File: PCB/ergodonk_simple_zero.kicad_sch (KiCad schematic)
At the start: 146 parts, among them J2 4PIN, Q1 TIP120, SW0 SW_PUSH_LED, SW08_RH10 SW_PUSH_LED, SW1 SW_PUSH_LED, SW10 SW_PUSH_LED, SW11 SW_PUSH_LED, SW12 SW_PUSH_LED, SW13 SW_PUSH_LED, SW14 SW_PUSH_LED, SW15 SW_PUSH_LED, SW16 SW_PUSH_LED, SW17 SW_PUSH_LED, SW18_RH10 SW_PUSH_LED, SW2 SW_PUSH_LED, SW20 SW_PUSH_LED, SW21 SW_PUSH_LED, SW22 SW_PUSH_LED, SW23 SW_PUSH_LED, SW24 SW_PUSH_LED, SW25 SW_PUSH_LED, SW26 SW_PUSH_LED, SW27 SW_PUSH_LED, SW28_RH10 SW_PUSH_LED, SW3 SW_PUSH_LED, SW30 SW_PUSH_LED, SW31 SW_PUSH_LED, SW32 SW_PUSH_LED, SW33 SW_PUSH_LED, SW34 SW_PUSH_LED, SW35 SW_PUSH_LED, SW36 SW_PUSH_LED, SW37 SW_PUSH_LED, SW38_RH10 SW_PUSH_LED, SW4 SW_PUSH_LED, SW40 SW_PUSH_LED, SW42 SW_PUSH_LED, SW43 SW_PUSH_LED, SW44 SW_PUSH_LED, SW45 SW_PUSH_LED, SW46 SW_PUSH_LED, SW47 SW_PUSH_LED, SW48_RH10 SW_PUSH_LED, SW5 SW_PUSH_LED, SW50 SW_PUSH_LED, SW51 SW_PUSH_LED, SW52 SW_PUSH_LED, SW53 SW_PUSH_LED, SW54 SW_PUSH_LED, SW55 SW_PUSH_LED, SW56 SW_PUSH_LED, SW57 SW_PUSH_LED, SW58 SW_PUSH_LED, SW6 SW_PUSH_LED, SW7 SW_PUSH_LED

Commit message: Added keycap labels updated RH exclusive component labels improved Solenoid circuit markings
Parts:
- J_SOL_1: footprint Connector_PinHeader_2.54mm:PinHeader_1x02_P2.54mm_Vertical -> Ergodonk_simple_zero:PinHeader_1x02_P2.54mm_Vertical
- R2: footprint Resistor_THT:R_Axial_DIN0309_L9.0mm_D3.2mm_P12.70mm_Horizontal -> Ergodonk_simple_zero:R_Axial_DIN0309_L9.0mm_D3.2mm_P12.70mm_Horizontal
- SW0: LH (none) -> VOL UP; RH (none) -> PRTSC
- SW08: renamed from SW08_RH10; RH (none) -> BKSP
- SW1: LH (none) -> F6; RH (none) -> F7
- SW10: LH (none) -> VOL DN; RH (none) -> SCRL
- SW11: LH (none) -> *; RH (none) -> INSERT
- SW12: LH (none) -> 5; RH (none) -> 6
- SW13: LH (none) -> 4; RH (none) -> 7
- SW14: LH (none) -> 3; RH (none) -> 8
- SW15: LH (none) -> 2; RH (none) -> 9
- SW16: LH (none) -> 1; RH (none) -> 0
- SW17: LH (none) -> `; RH (none) -> -
- SW18: renamed from SW18_RH10; RH (none) -> =
- SW2: LH (none) -> F5; RH (none) -> F8
- SW20: LH (none) -> MUTE; RH (none) -> PAUSE
- SW21: LH (none) -> PGUP; RH (none) -> DEL
- SW22: LH (none) -> T; RH (none) -> Y
- SW23: LH (none) -> R; RH (none) -> U
- SW24: LH (none) -> E; RH (none) -> I
- SW25: LH (none) -> W; RH (none) -> O
- SW26: LH (none) -> Q; RH (none) -> P
- SW27: LH (none) -> TAB; RH (none) -> [
- SW28: renamed from SW28_RH10; RH (none) -> \
- SW3: LH (none) -> F4; RH (none) -> F9
- SW30: LH (none) -> HOME; RH (none) -> PGUP
- SW31: LH (none) -> PGDN; RH (none) -> 5
- SW32: LH (none) -> G; RH (none) -> H
- SW33: LH (none) -> F; RH (none) -> I
- SW34: LH (none) -> D; RH (none) -> J
- SW35: LH (none) -> S; RH (none) -> K
- SW36: LH (none) -> A; RH (none) -> L
- SW37: LH (none) -> CAPS; RH (none) -> ;
- SW38: renamed from SW38_RH10; RH (none) -> ]
- SW4: LH (none) -> F3; RH (none) -> F10
- SW40: LH (none) -> END; RH (none) -> PGDN
- SW42: LH (none) -> B; RH (none) -> N
- SW43: LH (none) -> V; RH (none) -> M
- SW44: LH (none) -> C; RH (none) -> ,
- SW45: LH (none) -> X; RH (none) -> .
- SW46: LH (none) -> Z; RH (none) -> /
- SW47: LH (none) -> SHIFT; RH (none) -> SHIFT
- SW48: renamed from SW48_RH10; RH (none) -> ENTER
- SW5: LH (none) -> F2; RH (none) -> F11
- SW50: LH (none) -> 4; RH (none) -> 6
- SW51: LH (none) -> +; RH (none) -> SHIFT
- SW52: LH (none) -> 0; RH (none) -> ENTER
- SW53: LH (none) -> Fn; RH (none) -> ALT
- SW54: LH (none) -> →; RH (none) -> ↑
- SW55: LH (none) -> ←; RH (none) -> ↓
- SW56: LH (none) -> ALT; RH (none) -> Fn
- SW57: LH (none) -> WIN; RH (none) -> WIN
- SW58: LH (none) -> CTRL; RH (none) -> CTRL
- SW6: LH (none) -> F1; RH (none) -> F12
- SW7: LH (none) -> ESC; RH (none) -> DEL
- renumbered D08_RH10 to D08, D18_RH10 to D18, D28_RH10 to D28, D38_RH10 to D38, D48_RH10 to D48
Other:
- title: Ergodonk -> Ergodonk Zero
- moved on the sheet: D10, D11, D12, D13, D14, D15, D16, D17, D18, D20, D21, D22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

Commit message: Thumb key cluster footprint size change updated keyplate stab holes
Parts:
- SW51, SW52: footprint Ergodonk_simple_zero:CherryMX_Choc_Hotswap_ergodonk_simple_zero_DS -> Ergodonk_simple_zero:CherryMX_Choc_Hotswap_ergodonk_simple_zero_DS_2u_vert
- SW53: footprint Ergodonk_simple_zero:CherryMX_Choc_Hotswap_ergodonk_simple_zero_DS -> Ergodonk_simple_zero:CherryMX_Choc_Hotswap_ergodonk_simple_zero_DS_1.25u_vert
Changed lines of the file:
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@@
       (effects (font (size 1.27 1.27)))
     )
-    (property "Footprint" "Ergodonk_simple_zero:CherryMX_Choc_Hotswap_ergodonk_simple_zero_DS" (at 364.49 148.59 0)
+    (property "Footprint" "Ergodonk_simple_zero:CherryMX_Choc_Hotswap_ergodonk_simple_zero_DS_2u_vert" (at 364.49 148.59 0)
       (effects (font (size 1.27 1.27)) hide)
     )
@@
       (effects (font (size 1.27 1.27)))
     )
-    (property "Footprint" "Ergodonk_simple_zero:CherryMX_Choc_Hotswap_ergodonk_simple_zero_DS" (at 342.9 148.59 0)
+    (property "Footprint" "Ergodonk_simple_zero:CherryMX_Choc_Hotswap_ergodonk_simple_zero_DS_1.25u_vert" (at 342.9 148.59 0)
       (effects (font (size 1.27 1.27)) hide)
     )
@@
       (effects (font (size 1.27 1.27)))
     )
-    (property "Footprint" "Ergodonk_simple_zero:CherryMX_Choc_Hotswap_ergodonk_simple_zero_DS" (at 386.08 148.59 0)
-      (effects (font (size 1.27 1.27)) hide)
-    )
+    (property "Footprint" "Ergodonk_simple_zero:CherryMX_Choc_Hotswap_ergodonk_simple_zero_DS_2u_vert" (at 386.08 148.59 0)
+      (effects (font (size 1.27 1.27)) hide)
+    )

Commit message: Improved MCU markings Added keyplate cutout for solenoid
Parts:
- H20, H24: footprint Ergodonk_simple_zero:M2_Hole_fancy_for_bolt-on-plate -> Ergodonk_simple_zero:Hole from sofle for M2 posts gold rimmer
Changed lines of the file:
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@@
       (effects (font (size 1.27 1.27)) (justify left))
     )
-    (property "Footprint" "Ergodonk_simple_zero:M2_Hole_fancy_for_bolt-on-plate" (at 273.05 229.87 0)
+    (property "Footprint" "Ergodonk_simple_zero:Hole from sofle for M2 posts gold rimmer" (at 273.05 229.87 0)
       (effects (font (size 1.27 1.27)) hide)
     )
@@
       (effects (font (size 1.27 1.27)) (justify left))
     )
-    (property "Footprint" "Ergodonk_simple_zero:M2_Hole_fancy_for_bolt-on-plate" (at 251.46 260.35 0)
-      (effects (font (size 1.27 1.27)) hide)
-    )
+    (property "Footprint" "Ergodonk_simple_zero:Hole from sofle for M2 posts gold rimmer" (at 251.46 260.35 0)
+      (effects (font (size 1.27 1.27)) hide)
+    )

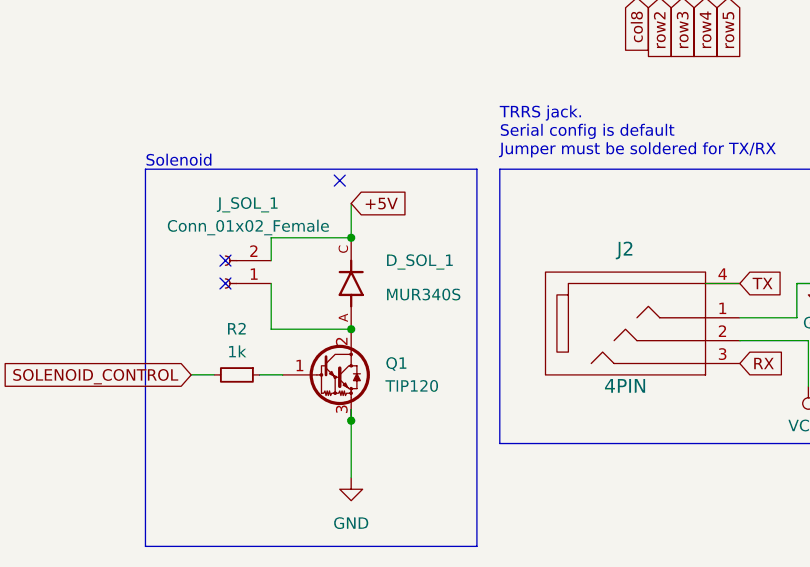
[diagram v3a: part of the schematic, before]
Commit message: Moved diodes to make more room for choc switches Improved In4004 markings and changed footprint
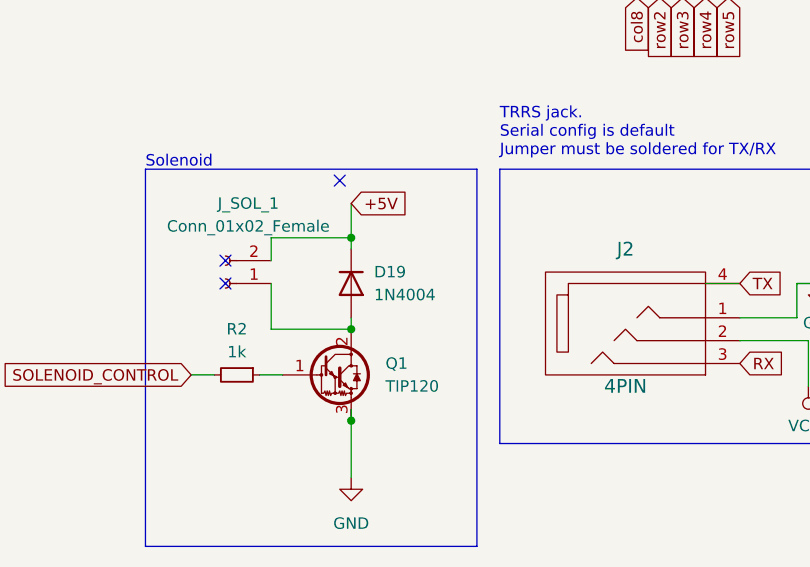
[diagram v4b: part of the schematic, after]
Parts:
- removed D_SOL_1: MUR340S, Ergodonk_simple_zero:MUR340S_IN4001_TH_HYBRID, symbol MUR340S:MUR340S
- added D19: 1N4004, Diode_THT:D_DO-41_SOD81_P10.16mm_Horizontal, symbol Diode:1N4004
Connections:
- net +5V: now also D19.1 (K)
- net at J_SOL_1.1 (Pin_1), Q1.2 (C): now also D19.2 (A)
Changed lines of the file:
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@@
   (junction (at 393.7 165.1) (diameter 0) (color 0 0 0 0)
   )
-  (junction (at 52.07 97.79) (diameter 0) (color 0 0 0 0)
-  )
   (junction (at 292.1 83.82) (diameter 0) (color 0 0 0 0)
   )
@@
   (junction (at 356.87 83.82) (diameter 0) (color 0 0 0 0)
   )
+  (junction (at 52.07 87.63) (diameter 0) (color 0 0 0 0)
+  )
   (junction (at 248.92 35.56) (diameter 0) (color 0 0 0 0)
   )
@@
   (junction (at 328.93 140.97) (diameter 0) (color 0 0 0 0)
   )
+  (junction (at 52.07 97.79) (diameter 0) (color 0 0 0 0)
+  )
   (junction (at 227.33 35.56) (diameter 0) (color 0 0 0 0)
   )
@@
   (junction (at 378.46 59.69) (diameter 0) (color 0 0 0 0)
   )
-  (junction (at 52.07 87.63) (diameter 0) (color 0 0 0 0)
-  )
   (junction (at 242.57 116.84) (diameter 0) (color 0 0 0 0)
   )
@@
     (stroke (width 0) (type default))
   )
+  (wire (pts (xy 52.07 96.52) (xy 52.07 97.79))
+    (stroke (width 0) (type default))
+  )
   (wire (pts (xy 248.92 59.69) (xy 248.92 83.82))
     (stroke (width 0) (type default))
@@
     (stroke (width 0) (type default))
   )
+  (wire (pts (xy 52.07 87.63) (xy 52.07 88.9))
+    (stroke (width 0) (type default))
+  )
   (polyline (pts (xy 29.21 121.92) (xy 66.04 121.92))
     (stroke (width 0) (type default))
@@
     )
   )
-  (symbol (lib_id "MUR340S:MUR340S") (at 52.07 92.71 90) (unit 1)
-    (in_bom yes) (on_board yes) (dnp no)
-    (property "Reference" "D_SOL_1" (at 55.88 90.17 90)
-      (effects (font (size 1.27 1.27)) (justify right))
-    )
-    (property "Value" "MUR340S" (at 55.88 93.98 90)
-      (effects (font (size 1.27 1.27)) (justify right))
-    )
-    (property "Footprint" "Ergodonk_simple_zero:MUR340S_IN4001_TH_HYBRID" (at 52.07 92.71 0)
-      (effects (font (size 1.27 1.27)) (justify bottom) hide)
-    )
-    (property "Datasheet" "" (at 52.07 92.71 0)
-      (effects (font (size 1.27 1.27)) hide)
-    )
-    (property "PARTREV" "L2102" (at 52.07 92.71 0)
-      (effects (font (size 1.27 1.27)) (justify bottom) hide)
-    )
-    (property "MANUFACTURER" "Taiwan Semiconductor" (at 52.07 92.71 0)
-      (effects (font (size 1.27 1.27)) (justify bottom) hide)
-    )
-    (property "MAXIMUM_PACKAGE_HEIGHT" "2.62 mm" (at 52.07 92.71 0)
-      (effects (font (size 1.27 1.27)) (justify bottom) hide)
-    )
-    (property "STANDARD" "IPC-7351B" (at 52.07 92.71 0)
-      (effects (font (size 1.27 1.27)) (justify bottom) hide)
-    )
-    (pin "A")
-    (pin "C")
-    (instances
-      (project "ergodonk_simple_zero"
-        (path "/ed1aaf15-4e1f-4159-b371-d99b3fb972ad"
-          (reference "D_SOL_1") (unit 1)
-        )
-      )
-    )
-  )
   (symbol (lib_id "Mechanical:MountingHole") (at 223.52 219.71 0) (unit 1)
     (in_bom yes) (on_board yes) (dnp no) (fields_autoplaced)
@@
         )
       )
+    )
+  )
+  (symbol (lib_id "Diode:1N4004") (at 52.07 92.71 270) (unit 1)
+    (in_bom yes) (on_board yes) (dnp no) (fields_autoplaced)
+    (property "Reference" "D19" (at 54.61 91.44 90)
+      (effects (font (size 1.27 1.27)) (justify left))
+    )
+    (property "Value" "1N4004" (at 54.61 93.98 90)
+      (effects (font (size 1.27 1.27)) (justify left))
+    )
+    (property "Footprint" "Diode_THT:D_DO-41_SOD81_P10.16mm_Horizontal" (at 47.625 92.71 0)
+      (effects (font (size 1.27 1.27)) hide)
+    )
+    (property "Datasheet" "http://www.vishay.com/docs/88503/1n4001.pdf" (at 52.07 92.71 0)
+      (effects (font (size 1.27 1.27)) hide)
+    )
+    (property "Sim.Device" "D" (at 52.07 92.71 0)
+      (effects (font (size 1.27 1.27)) hide)
+    )
+    (property "Sim.Pins" "1=K 2=A" (at 52.07 92.71 0)
+      (effects (font (size 1.27 1.27)) hide)
+    )
+    (pin "1")
+    (pin "2")
+    (instances
+      (project "ergodonk_simple_zero"
+        (path "/ed1aaf15-4e1f-4159-b371-d99b3fb972ad"
+          (reference "D19") (unit 1)
+        )
+      )

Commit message: Added bending jigs Removed pin 1 markings from solenoid footprint
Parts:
- D19: footprint Diode_THT:D_DO-41_SOD81_P10.16mm_Horizontal -> Ergodonk_simple_zero:D_DO-41_SOD81_P10.16mm_Horizontal
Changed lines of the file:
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@@
       (effects (font (size 1.27 1.27)) (justify left))
     )
-    (property "Footprint" "Diode_THT:D_DO-41_SOD81_P10.16mm_Horizontal" (at 47.625 92.71 0)
+    (property "Footprint" "Ergodonk_simple_zero:D_DO-41_SOD81_P10.16mm_Horizontal" (at 47.625 92.71 0)
       (effects (font (size 1.27 1.27)) hide)
     )

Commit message: Updated TRRS jack location experimented with collapsing tRRS to TRS. (Decided against it)
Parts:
- J2: footprint ergodonk_kicad_library:MJ-4PP-9_CANTOR_KITCHEN_SINK -> Ergodonk_simple_zero:MJ-4PP-9_TRRS_ds_jack
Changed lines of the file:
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@@
       (effects (font (size 1.524 1.524)))
     )
-    (property "Footprint" "ergodonk_kicad_library:MJ-4PP-9_CANTOR_KITCHEN_SINK" (at 83.82 97.79 0)
+    (property "Footprint" "Ergodonk_simple_zero:MJ-4PP-9_TRRS_ds_jack" (at 83.82 97.79 0)
       (effects (font (size 1.524 1.524)) hide)
     )

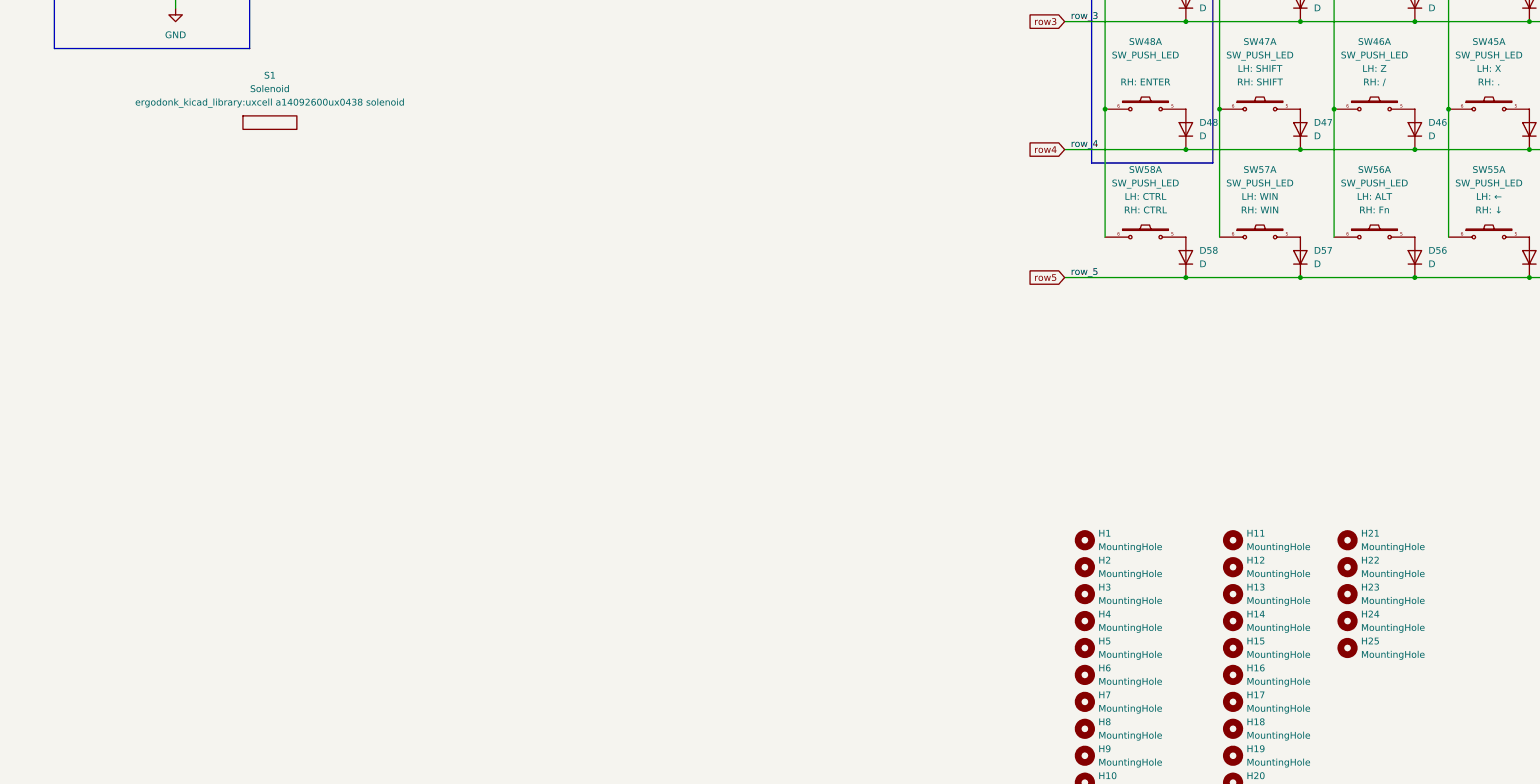
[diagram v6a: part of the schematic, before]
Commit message: Built solenoid plates Revised key plates Moved mounting holes to minimize or showcase THIS VERSION WAS SENT OUT FOR PRODUCTION ON 1-11-2024
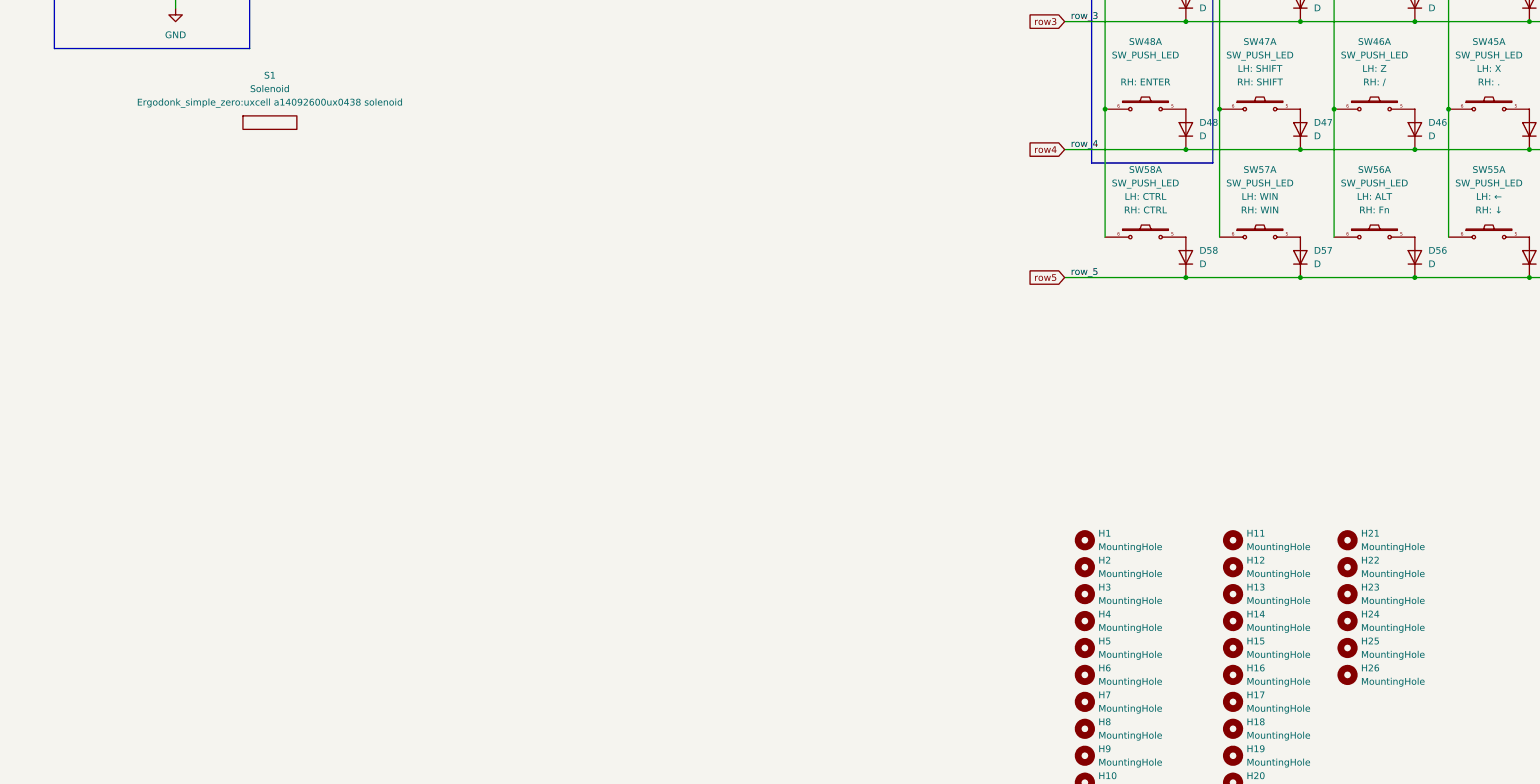
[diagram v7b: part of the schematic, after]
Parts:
- added H26: MountingHole, Ergodonk_simple_zero:Hole from sofle for M2 posts gold rimmer, symbol Mechanical:MountingHole
- S1: footprint ergodonk_kicad_library:uxcell a14092600ux0438 solenoid -> Ergodonk_simple_zero:uxcell a14092600ux0438 solenoid
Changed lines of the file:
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@@
+    )
+  )
+  (symbol (lib_id "Mechanical:MountingHole") (at 273.05 240.03 0) (unit 1)
+    (in_bom yes) (on_board yes) (dnp no) (fields_autoplaced)
+    (property "Reference" "H26" (at 275.59 238.7599 0)
+      (effects (font (size 1.27 1.27)) (justify left))
+    )
+    (property "Value" "MountingHole" (at 275.59 241.2999 0)
+      (effects (font (size 1.27 1.27)) (justify left))
+    )
+    (property "Footprint" "Ergodonk_simple_zero:Hole from sofle for M2 posts gold rimmer" (at 273.05 240.03 0)
+      (effects (font (size 1.27 1.27)) hide)
+    )
+    (property "Datasheet" "~" (at 273.05 240.03 0)
+      (effects (font (size 1.27 1.27)) hide)
+    )
+    (instances
+      (project "ergodonk_simple_zero"
+        (path "/ed1aaf15-4e1f-4159-b371-d99b3fb972ad"
+          (reference "H26") (unit 1)
+        )
+      )
     )
   )
@@
       (effects (font (size 1.27 1.27)))
     )
-    (property "Footprint" "ergodonk_kicad_library:uxcell a14092600ux0438 solenoid" (at 69.85 132.08 0)
-      (effects (font (size 1.27 1.27)))
-    )
+    (property "Footprint" "Ergodonk_simple_zero:uxcell a14092600ux0438 solenoid" (at 69.85 132.08 0)
+      (effects (font (size 1.27 1.27)))
+    )
